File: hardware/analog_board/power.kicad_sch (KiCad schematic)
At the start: 99 parts, among them U10 TPS54360DDA, U11 TPS62933, U12 L7805, U13 L7905, U14 TPS7A4701xRGW, U15 TPS7A91, U16 L7815, U17 L7915, U19 AMS1117, U9 TPS54360DDA

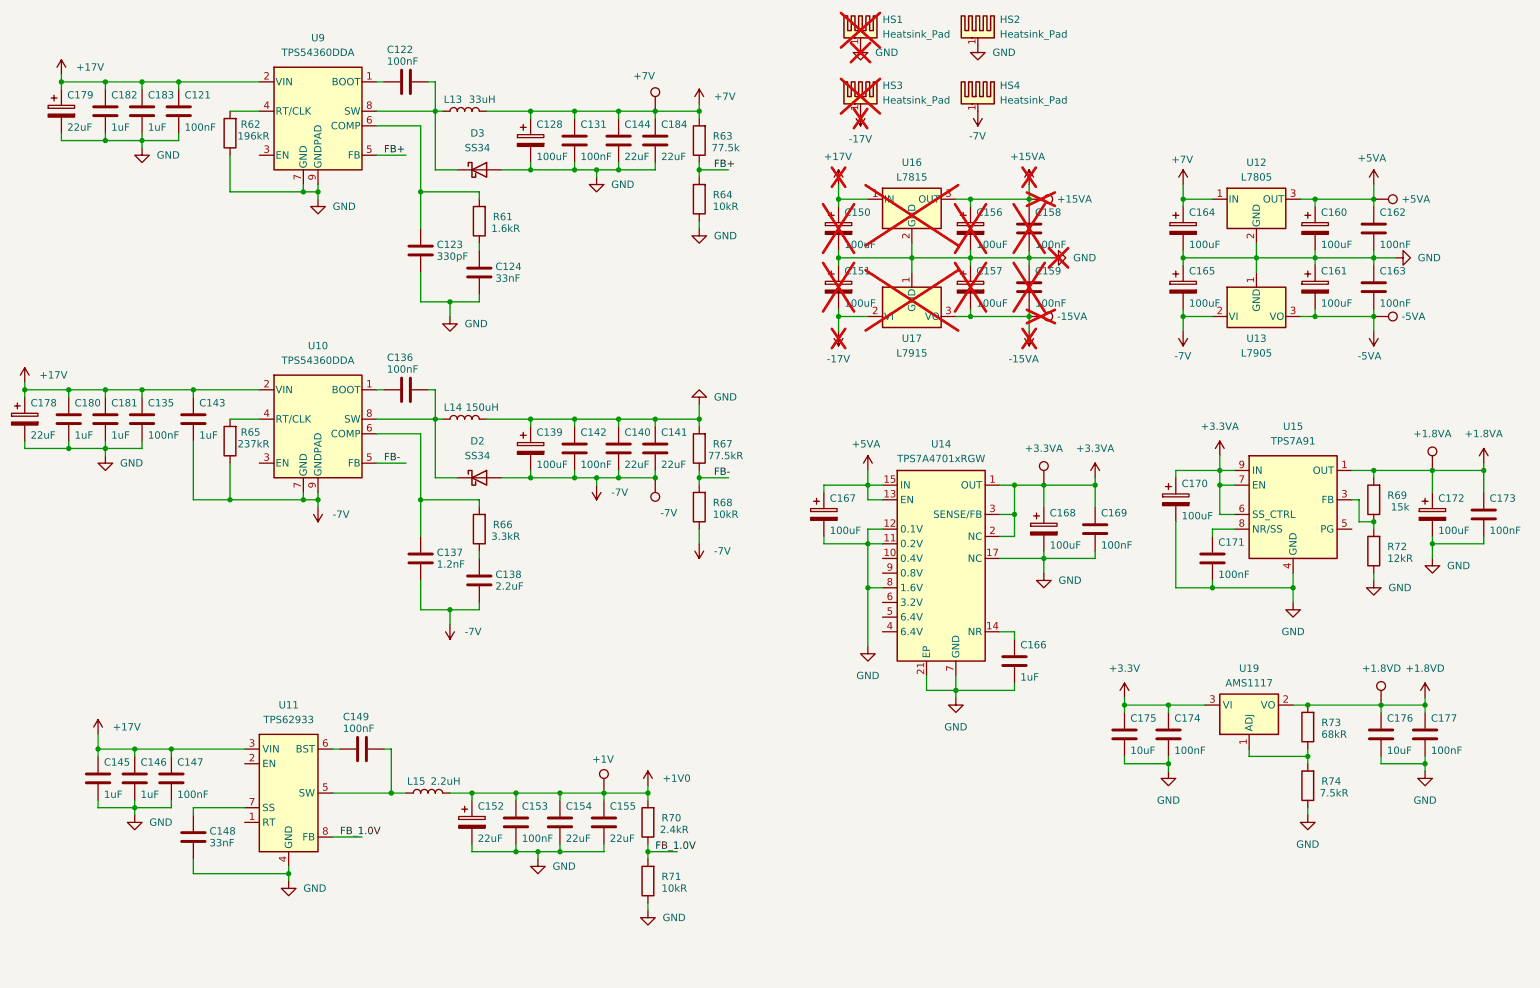
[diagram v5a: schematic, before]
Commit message: feat：±7V电源移动到控制板（原理图修改）
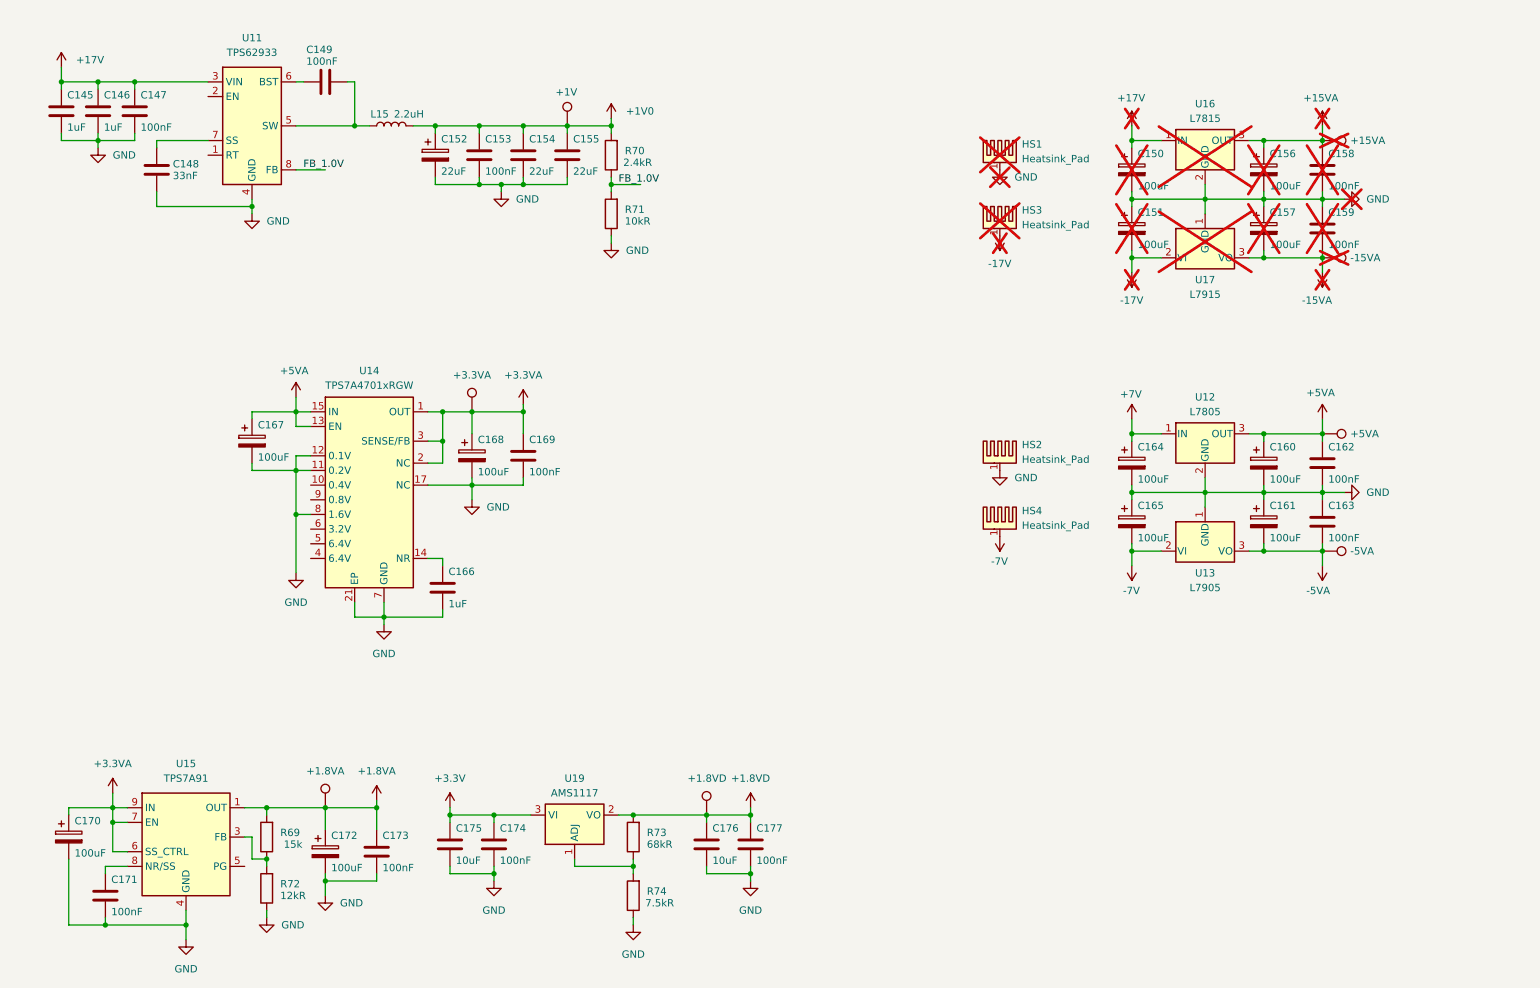
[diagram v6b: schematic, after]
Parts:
- removed C121, C122, C131, C135, C136, C142: 100nF, Capacitor_SMD:C_0603_1608Metric, symbol Device:C
- removed C123: 330pF, Capacitor_SMD:C_0603_1608Metric, symbol Device:C
- removed C124: 33nF, Capacitor_SMD:C_0603_1608Metric, symbol Device:C
- removed C128, C139: 100uF, Capacitor_SMD:C_Elec_6.3x7.7, symbol Device:C_Polarized
- removed C137: 1.2nF, Capacitor_SMD:C_0603_1608Metric, symbol Device:C
- removed C138: 2.2uF, Capacitor_SMD:C_0603_1608Metric, symbol Device:C
- removed C140, C141, C144, C184: 22uF, Capacitor_SMD:C_1206_3216Metric, symbol Device:C
- removed C143: 1uF, Capacitor_SMD:C_0603_1608Metric, symbol Device:C
- removed C178, C179: 22uF, Capacitor_SMD:CP_Elec_5x5.4, symbol Device:C_Polarized
- removed C180, C181, C182, C183: 1uF, Capacitor_SMD:C_1206_3216Metric, symbol Device:C
- removed D2, D3: SS34, Diode_SMD:D_SMA, symbol Diode:SS34
- removed L13: 33uH, Inductor_SMD:L_Changjiang_FXL1040, symbol Device:L
- removed L14: 150uH, Inductor_SMD:L_12x12mm_H6mm, symbol Device:L
- removed R61: 1.6kR, Resistor_SMD:R_0603_1608Metric, symbol Device:R
- removed R62: 196kR, Resistor_SMD:R_0603_1608Metric, symbol Device:R
- removed R63: 77.5k, Resistor_SMD:R_0603_1608Metric, symbol Device:R
- removed R64, R68: 10kR, Resistor_SMD:R_0603_1608Metric, symbol Device:R
- removed R65: 237kR, Resistor_SMD:R_0603_1608Metric, symbol Device:R
- removed R66: 3.3kR, Resistor_SMD:R_0603_1608Metric, symbol Device:R
- removed R67: 77.5kR, Resistor_SMD:R_0603_1608Metric, symbol Device:R
- removed TP10: -7V, TestPoint:TestPoint_Pad_D1.0mm, symbol Connector:TestPoint
- removed TP9: +7V, TestPoint:TestPoint_Pad_D1.0mm, symbol Connector:TestPoint
- removed U10, U9: TPS54360DDA, Package_SO:TI_SO-PowerPAD-8_ThermalVias, symbol Regulator_Switching:TPS54360DDA
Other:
- moved on the sheet: C150, C151, C156, C157, C158, C159, C160, C161, C162, C163, C164, C165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

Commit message: feat：导出模拟板 BOM
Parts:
- TP11, TP12, TP13, TP14, TP15, TP16, TP17, TP18: now left out of the parts list
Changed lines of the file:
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@@
 		(body_style 1)
 		(exclude_from_sim no)
-		(in_bom yes)
+		(in_bom no)
 		(on_board yes)
 		(in_pos_files yes)
@@
 		(body_style 1)
 		(exclude_from_sim no)
-		(in_bom yes)
+		(in_bom no)
 		(on_board no)
 		(in_pos_files yes)
@@
 		(body_style 1)
 		(exclude_from_sim no)
-		(in_bom yes)
+		(in_bom no)
 		(on_board yes)
 		(in_pos_files yes)
@@
 		(body_style 1)
 		(exclude_from_sim no)
-		(in_bom yes)
+		(in_bom no)
 		(on_board yes)
 		(in_pos_files yes)
@@
 		(body_style 1)
 		(exclude_from_sim no)
-		(in_bom yes)
+		(in_bom no)
 		(on_board no)
 		(in_pos_files yes)
@@
 		(body_style 1)
 		(exclude_from_sim no)
-		(in_bom yes)
+		(in_bom no)
 		(on_board yes)
 		(in_pos_files yes)
@@
 		(body_style 1)
 		(exclude_from_sim no)
-		(in_bom yes)
+		(in_bom no)
 		(on_board yes)
 		(in_pos_files yes)
@@
 		(body_style 1)
 		(exclude_from_sim no)
-		(in_bom yes)
+		(in_bom no)
 		(on_board yes)
 		(in_pos_files yes)
